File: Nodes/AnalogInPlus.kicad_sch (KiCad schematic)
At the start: 2 parts, among them J7 HLE-104-02-L-DV-BE-A-P-TR, J8 HLE-104-02-L-DV-BE-A-P-TR

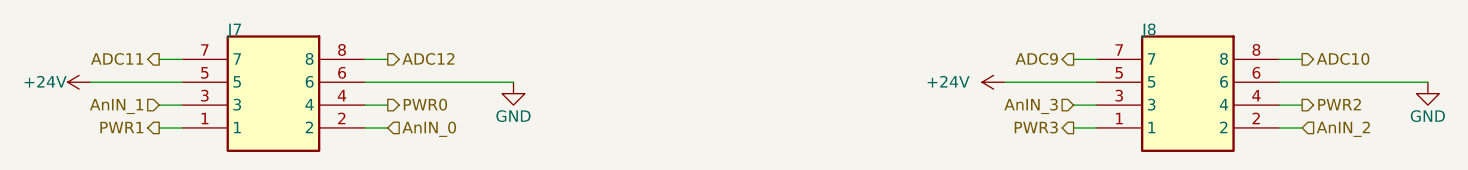
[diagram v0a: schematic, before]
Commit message: Nodes v2.1.2 Improved
- Improved schematic design
- Added two 4.7 uF caps according to the datasheets of the microchips
- Other small changes
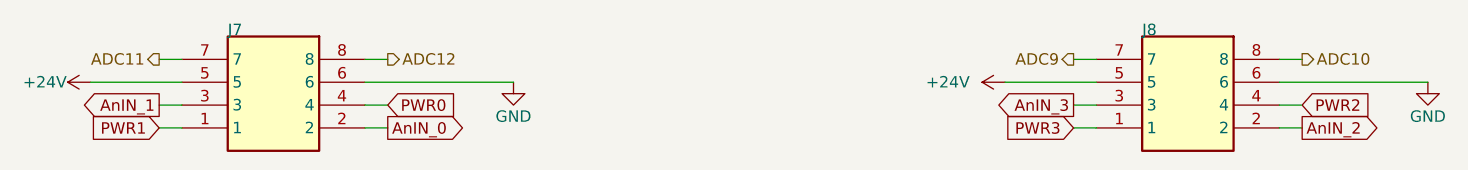
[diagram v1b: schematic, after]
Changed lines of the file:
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@@
 		)
 	)
-	(hierarchical_label "PWR2"
-		(shape output)
+	(global_label "AnIN_3"
+		(shape output)
+		(at 180.34 101.6 180)
+		(fields_autoplaced yes)
+		(effects
+			(font
+				(size 1.27 1.27)
+			)
+			(justify right)
+		)
+		(property "Intersheetrefs" "${INTERSHEET_REFS}"
+			(at 171.0048 101.6 0)
+			(effects
+				(font
+					(size 1.27 1.27)
+				)
+				(justify right)
+				(hide yes)
+			)
+		)
+	)
+	(global_label "PWR3"
+		(shape input)
+		(at 180.34 104.14 180)
+		(fields_autoplaced yes)
+		(effects
+			(font
+				(size 1.27 1.27)
+			)
+			(justify right)
+		)
+		(property "Intersheetrefs" "${INTERSHEET_REFS}"
+			(at 172.1539 104.14 0)
+			(effects
+				(font
+					(size 1.27 1.27)
+				)
+				(justify right)
+				(hide yes)
+			)
+		)
+	)
+	(global_label "AnIN_1"
+		(shape output)
+		(at 78.74 101.6 180)
+		(fields_autoplaced yes)
+		(effects
+			(font
+				(size 1.27 1.27)
+			)
+			(justify right)
+		)
+		(property "Intersheetrefs" "${INTERSHEET_REFS}"
+			(at 69.4048 101.6 0)
+			(effects
+				(font
+					(size 1.27 1.27)
+				)
+				(justify right)
+				(hide yes)
+			)
+		)
+	)
+	(global_label "AnIN_0"
+		(shape output)
+		(at 104.14 104.14 0)
+		(fields_autoplaced yes)
+		(effects
+			(font
+				(size 1.27 1.27)
+			)
+			(justify left)
+		)
+		(property "Intersheetrefs" "${INTERSHEET_REFS}"
+			(at 113.4752 104.14 0)
+			(effects
+				(font
+					(size 1.27 1.27)
+				)
+				(justify left)
+				(hide yes)
+			)
+		)
+	)
+	(global_label "PWR0"
+		(shape input)
+		(at 104.14 101.6 0)
+		(fields_autoplaced yes)
+		(effects
+			(font
+				(size 1.27 1.27)
+			)
+			(justify left)
+		)
+		(property "Intersheetrefs" "${INTERSHEET_REFS}"
+			(at 112.3261 101.6 0)
+			(effects
+				(font
+					(size 1.27 1.27)
+				)
+				(justify left)
+				(hide yes)
+			)
+		)
+	)
+	(global_label "PWR1"
+		(shape input)
+		(at 78.74 104.14 180)
+		(fields_autoplaced yes)
+		(effects
+			(font
+				(size 1.27 1.27)
+			)
+			(justify right)
+		)
+		(property "Intersheetrefs" "${INTERSHEET_REFS}"
+			(at 70.5539 104.14 0)
+			(effects
+				(font
+					(size 1.27 1.27)
+				)
+				(justify right)
+				(hide yes)
+			)
+		)
+	)
+	(global_label "AnIN_2"
+		(shape output)
+		(at 205.74 104.14 0)
+		(fields_autoplaced yes)
+		(effects
+			(font
+				(size 1.27 1.27)
+			)
+			(justify left)
+		)
+		(property "Intersheetrefs" "${INTERSHEET_REFS}"
+			(at 215.0752 104.14 0)
+			(effects
+				(font
+					(size 1.27 1.27)
+				)
+				(justify left)
+				(hide yes)
+			)
+		)
+	)
+	(global_label "PWR2"
+		(shape input)
 		(at 205.74 101.6 0)
 		(fields_autoplaced yes)
@@
 			(justify left)
 		)
+		(property "Intersheetrefs" "${INTERSHEET_REFS}"
+			(at 213.9261 101.6 0)
+			(effects
+				(font
+					(size 1.27 1.27)
+				)
+				(justify left)
+				(hide yes)
+			)
+		)
 	)
 	(hierarchical_label "ADC10"
@@
 		)
 	)
-	(hierarchical_label "PWR0"
-		(shape output)
-		(at 104.14 101.6 0)
-		(fields_autoplaced yes)
-		(effects
-			(font
-				(size 1.27 1.27)
-			)
-			(justify left)
-		)
-	)
 	(hierarchical_label "ADC12"
 		(shape output)
@@
 		)
 	)
-	(hierarchical_label "AnIN_3"
-		(shape input)
-		(at 180.34 101.6 180)
-		(fields_autoplaced yes)
-		(effects
-			(font
-				(size 1.27 1.27)
-			)
-			(justify right)
-		)
-	)
-	(hierarchical_label "PWR1"
-		(shape output)
-		(at 78.74 104.14 180)
-		(fields_autoplaced yes)
-		(effects
-			(font
-				(size 1.27 1.27)
-			)
-			(justify right)
-		)
-	)
 	(hierarchical_label "ADC11"
 		(shape output)
@@
 		)
 	)
-	(hierarchical_label "AnIN_2"
-		(shape input)
-		(at 205.74 104.14 0)
-		(fields_autoplaced yes)
-		(effects
-			(font
-				(size 1.27 1.27)
-			)
-			(justify left)
-		)
-	)
-	(hierarchical_label "AnIN_1"
-		(shape input)
-		(at 78.74 101.6 180)
-		(fields_autoplaced yes)
-		(effects
-			(font
-				(size 1.27 1.27)
-			)
-			(justify right)
-		)
-	)
-	(hierarchical_label "PWR3"
-		(shape output)
-		(at 180.34 104.14 180)
-		(fields_autoplaced yes)
-		(effects
-			(font
-				(size 1.27 1.27)
-			)
-			(justify right)
-		)
-	)
 	(hierarchical_label "ADC9"
 		(shape output)
@@
 		)
 	)
-	(hierarchical_label "AnIN_0"
-		(shape input)
-		(at 104.14 104.14 0)
-		(fields_autoplaced yes)
-		(effects
-			(font
-				(size 1.27 1.27)
-			)
-			(justify left)
-		)
-	)
